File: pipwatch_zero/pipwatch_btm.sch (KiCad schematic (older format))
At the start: 2 parts, among them U501 BTM431

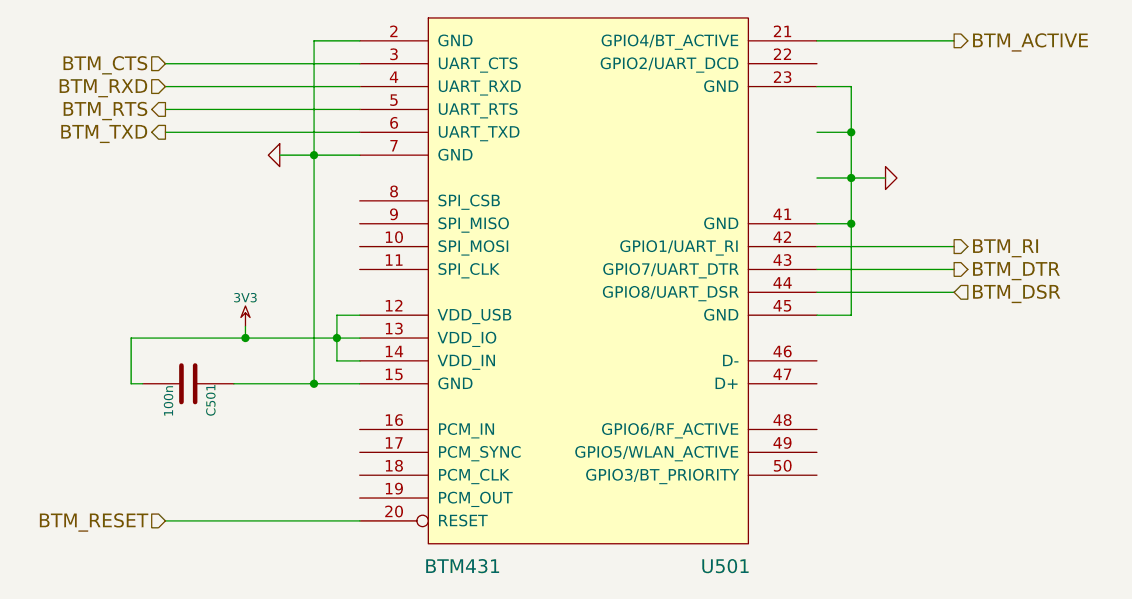
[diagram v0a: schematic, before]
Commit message: pipwatch_zero: footprints
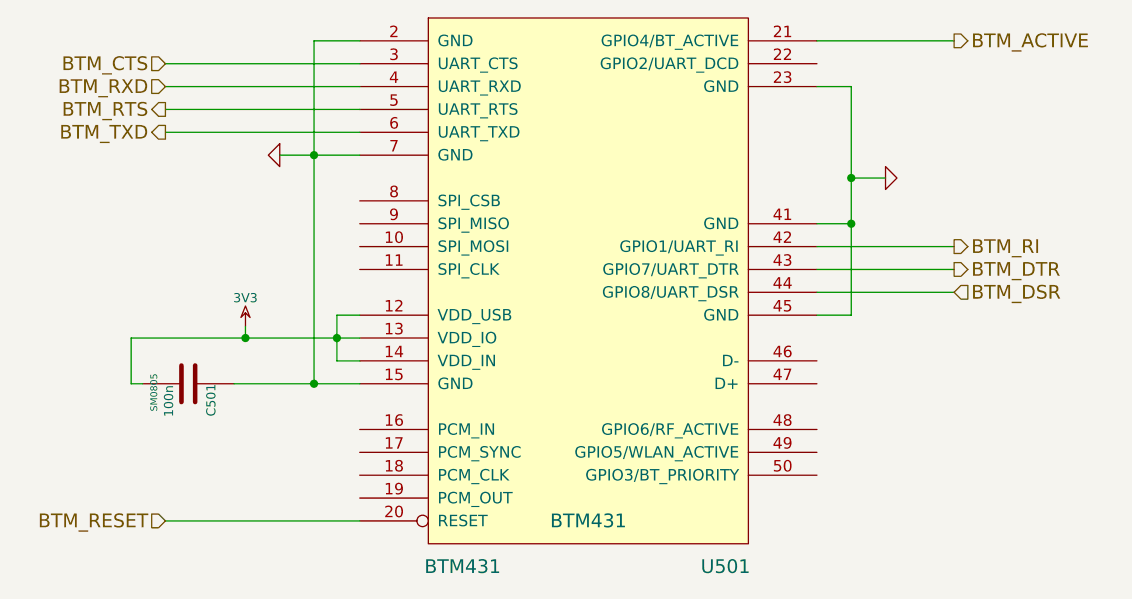
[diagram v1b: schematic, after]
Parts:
- C501: footprint (none) -> SM0805
- U501: footprint (none) -> BTM431
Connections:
- wire segments 26 -> 25
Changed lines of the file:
@@
 Sheet 5 5
 Title ""
-Date "23 aug 2014"
+Date "24 aug 2014"
 Rev ""
 Comp ""
@@
 F 0 "U501" H 6000 4300 60  0000 C CNN
 F 1 "BTM431" H 4850 4300 60  0000 C CNN
-F 2 "" H 5400 4500 60  0000 C CNN
+F 2 "BTM431" H 5400 4500 60  0000 C CNN
 F 3 "" H 5400 4500 60  0000 C CNN
 	1    5400 4500
@@
 	6550 2600 6550 3600
 Wire Wire Line
-	6400 3000 6700 3000
-Wire Wire Line
-	6400 2800 6550 2800
-Connection ~ 6550 2800
-Wire Wire Line
 	6550 3200 6400 3200
-Connection ~ 6550 3000
 Wire Wire Line
 	6550 3600 6400 3600
 Connection ~ 6550 3200
 $Comp
-L GND #PWR041
+L GND #PWR046
 U 1 1 53EF6996
 P 4050 2900
-F 0 "#PWR041" H 4050 2900 30  0001 C CNN
+F 0 "#PWR046" H 4050 2900 30  0001 C CNN
 F 1 "GND" H 4050 2830 30  0001 C CNN
 F 2 "" H 4050 2900 60  0000 C CNN
@@
 $EndComp
 $Comp
-L GND #PWR042
+L GND #PWR047
 U 1 1 53EF69AA
 P 6700 3000
-F 0 "#PWR042" H 6700 3000 30  0001 C CNN
+F 0 "#PWR047" H 6700 3000 30  0001 C CNN
 F 1 "GND" H 6700 2930 30  0001 C CNN
 F 2 "" H 6700 3000 60  0000 C CNN
@@
 Connection ~ 4300 3700
 $Comp
-L 3V3 #PWR043
+L 3V3 #PWR048
 U 1 1 53EF6A0E
 P 3900 3650
-F 0 "#PWR043" H 3900 3750 40  0001 C CNN
+F 0 "#PWR048" H 3900 3750 40  0001 C CNN
 F 1 "3V3" H 3900 3775 40  0000 C CNN
 F 2 "" H 3900 3650 60  0000 C CNN
@@
 F 0 "C501" H 3650 4000 40  0000 L CNN
 F 1 "100n" H 3656 3815 40  0000 L CNN
-F 2 "" H 3688 3750 30  0000 C CNN
+F 2 "SM0805" H 3688 3750 30  0000 C CNN
 F 3 "" H 3650 3900 60  0000 C CNN
 	1    3650 3900
@@
 	3400 3900 3450 3900
 Connection ~ 3900 3700
+Wire Wire Line
+	6700 3000 6550 3000
+Connection ~ 6550 3000
 $EndSCHEMATC
